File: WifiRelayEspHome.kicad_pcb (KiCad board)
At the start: 2 copper layers, 50.5 x 72.1 mm, 28 parts, among them J1 Conn_01x03, J2 Conn_01x03, J3 Barrel_Jack, J4 FTDI_Cable, K1 G5LE-14_DC3, K2 G5LE-14_DC3, Q1 2N3904, Q2 2N3904, SW1 GND_to_reset, SW2 GND_to_program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

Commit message: Added github link to silkscren
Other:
- board text added: "https://github.com/CindyPotvin/WifiRelayESPHome"
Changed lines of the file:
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@@
   (general
     (thickness 1.6)
-    (drawings 21)
+    (drawings 22)
     (tracks 136)
     (zones 0)
@@
       (drillshape 0)
       (scaleselection 1)
-      (outputdirectory "TemperatureLogger_ESP-12F_Gerber/"))
+      (outputdirectory "WifiRelayEspHome_Gerber/"))
   )
   (net 0 "")
@@
     )
   )
+  (gr_text https://github.com/CindyPotvin/WifiRelayESPHome (at 156.2718 123.7356 90) (layer B.SilkS)
+    (effects (font (size 0.8 0.8) (thickness 0.15)) (justify mirror))
+  )
   (gr_text COM (at 150.7346 76.9488) (layer F.SilkS)
     (effects (font (size 0.8 0.8) (thickness 0.15)))
@@
     (effects (font (size 0.8 0.8) (thickness 0.15)))
   )
-  (gr_text "Relais pour ESPHome\nMAX 120VAC/120VDC \n5A\nCindy Potvin\nv1.0" (at 149.0074 125.8184 90) (layer B.SilkS)
+  (gr_text "Relais pour ESPHome\nMAX 120VAC/120VDC \n5A\nCindy Potvin\nv1.0\n" (at 149.0074 125.8184 90) (layer B.SilkS)
     (effects (font (size 1.5 1.5) (thickness 0.3)) (justify mirror))
   )

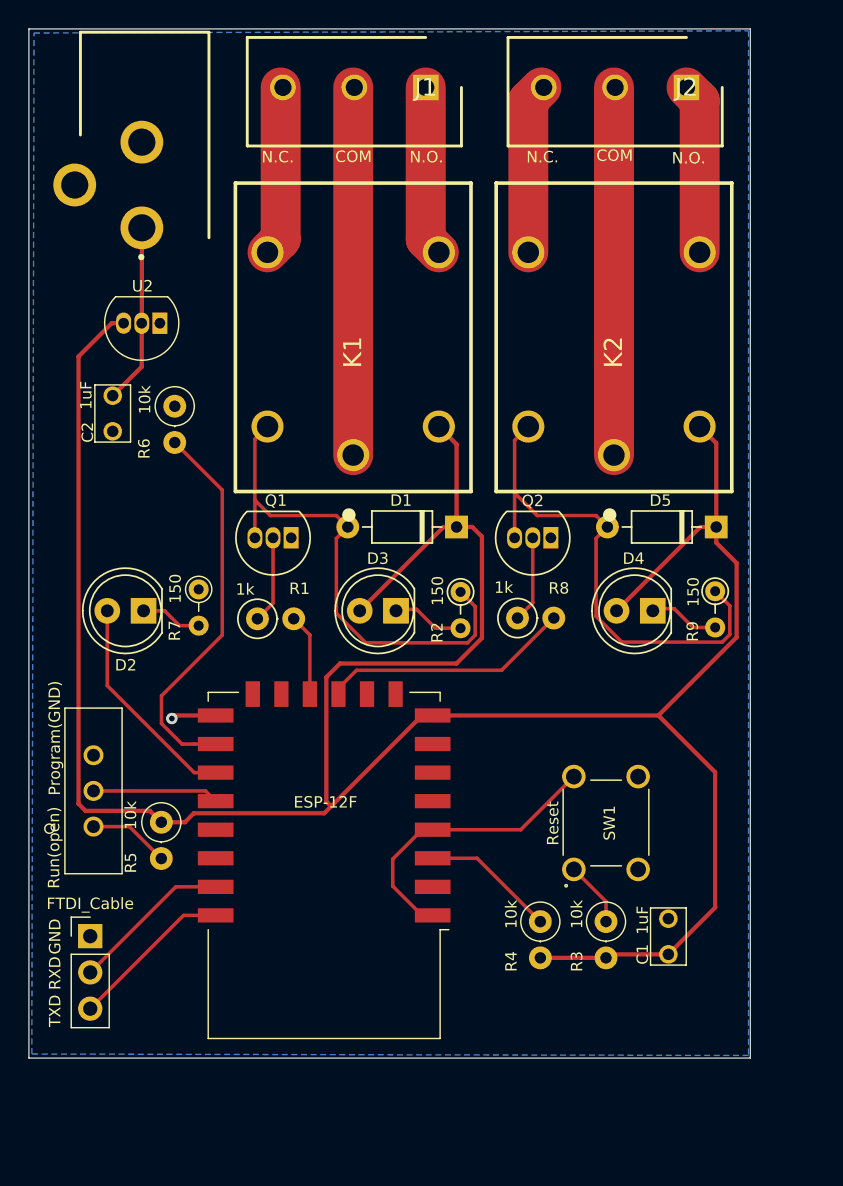
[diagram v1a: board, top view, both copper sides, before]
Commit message: Final version after testing: changed pins, moved barrel jack and added mounting holes
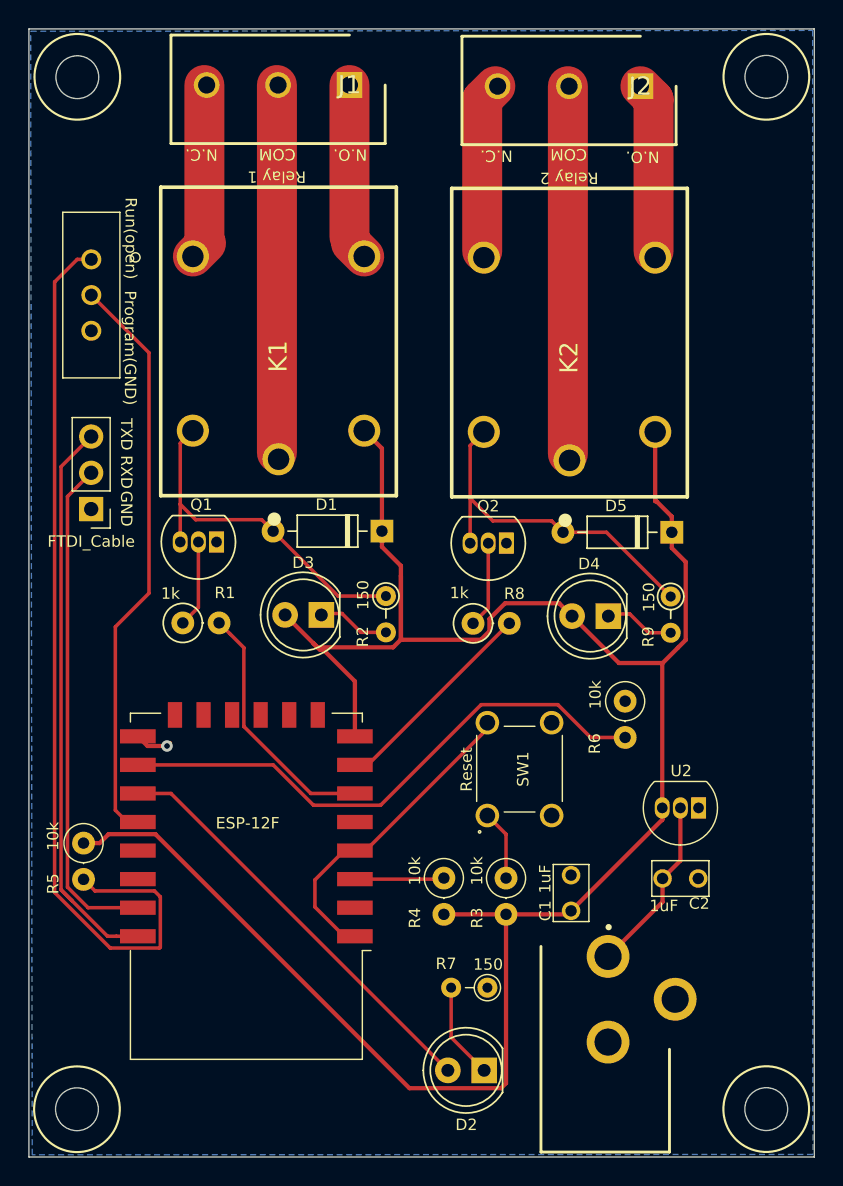
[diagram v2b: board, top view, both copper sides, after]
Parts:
- moved J3 70.4 mm to (172.9, 136.0), turned to 180 degrees
- moved C2 51.4 mm to (173.6, 127.5), turned to 0 degrees
- moved U2 50.7 mm to (174.9, 122.6)
- moved D2 40.1 mm to (159.9, 140.9)
- moved R6 37.7 mm to (169.8, 115.1)
- moved SW2 34.7 mm to (132.4, 86.6), turned to 270 degrees
- moved R7 34.4 mm to (160.1, 135.1), turned to 180 degrees
- moved J4 29.9 mm to (132.4, 101.6), turned to 180 degrees
- moved R3 7.63 mm to (161.4, 127.5)
- moved C1 7.46 mm to (166.0, 128.5)
- moved R4 7.41 mm to (157.1, 127.5)
- moved SW1 7.14 mm to (162.4, 119.8)
- moved R5 5.64 mm to (131.8, 125.0)
- moved U1 5.64 mm to (143.2, 128.0)
- moved J1 5.34 mm to (150.4, 71.9)
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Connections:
- U1 pad 11: /RELAY2 -> (no net)
- U1 pad 12: /RELAY1 -> (no net)
- U1 pad 6: (no net) -> /RELAY1
- U1 pad 7: (no net) -> /RELAY2
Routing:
- net Net-(R5-Pad2): track 5.68 -> 64.4 mm
- net /3.3V: track 188.6 -> 156.5 mm
- net Net-(SW2-Pad2): track 8.85 -> 40.6 mm
- net /TXD: track 11.9 -> 41.5 mm
- net /RXD: track 11.7 -> 37.1 mm
- net Net-(D2-Pad2): track 15.4 -> 29.7 mm
- net Net-(R6-Pad2): track 27.2 -> 39.2 mm
- net /RELAY1: track 6.14 -> 17.7 mm
- net Net-(D5-Pad2): track 36.1 -> 25.1 mm
- net Net-(D1-Pad2): track 36.1 -> 25.2 mm
- net Net-(R4-Pad1): track 9.37 -> 6.26 mm
- net Net-(D2-Pad1): track 4.29 -> 6.75 mm
- net /RELAY2: track 17.5 -> 15.7 mm
- net /WAKE: track 21.4 -> 22.4 mm
- net Earth: track 3.16 -> 2.62 mm
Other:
- board size 50.5 x 72.1 mm -> 55 x 79 mm
- board text added: "Relais pour ESPHome MAX 120VAC/120VDC 5A Cindy Potvin v1.2"
- board text added: "Relay 1"
- board text added: "Relay 2"
- board text removed: "Relais pour ESPHome MAX 120VAC/120VDC 5A Cindy Potvin v1.0"
